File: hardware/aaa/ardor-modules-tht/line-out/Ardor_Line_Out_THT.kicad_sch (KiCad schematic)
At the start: 27 parts, among them J101 5V POWER + ENABLE INPUT, J102 MONO AUDIO INPUT FROM SOURCE, J502 AUDIO OUTPUT TO AMP INPUT, J503 LINE AUDIO OUTPUT TO TS SOCKET, K501 Omron G5V-1 DC5, Q501 2N3904 / E-B-C, U501 MCP6022-I/P

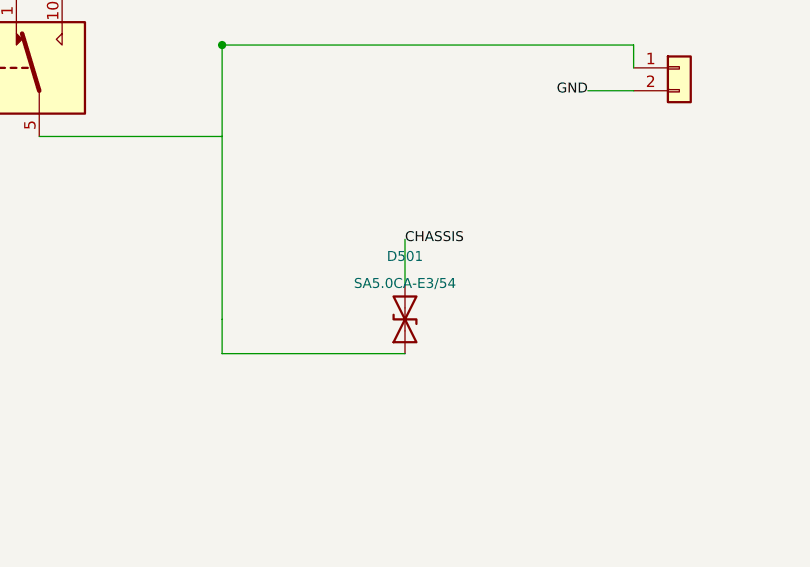
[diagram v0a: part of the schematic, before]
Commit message: fix(hardware): use Hestore TVS diodes in hand-assembly modules
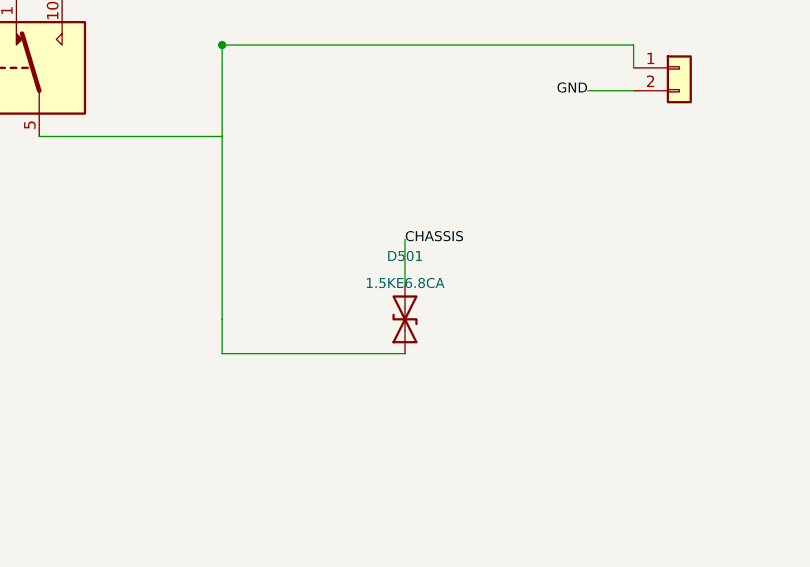
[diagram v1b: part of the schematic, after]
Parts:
- D501: value SA5.0CA-E3/54 -> 1.5KE6.8CA; footprint Diode_THT:D_DO-15_P10.16mm_Horizontal -> Ardor_THT:D_TVS_DC_1.5KE_P15.24mm; MPN Vishay SA5.0CA-E3/54 -> DC Components 1.5KE6.8CA (HESTORE 100.430.71)

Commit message: feat(hardware): compact layouts and adopt Hestore module packages
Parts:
- C401, C502: value 10u / 25V BIPOLAR -> 10u / 50V BIPOLAR; footprint Ardor_THT:CP_Bipolar_D6.3mm_P2.50mm -> Ardor_THT:CP_Bipolar_Nichicon_D8.0mm_P3.50mm; MPN Nichicon UES1E100MDM -> Nichicon UES1H100MPM (HESTORE 100.524.69)
